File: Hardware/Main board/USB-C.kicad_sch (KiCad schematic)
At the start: 2 parts, among them P1 USB_C_Plug_USB2.0

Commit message: Big changes
- Folder changes
- change dimensions of board to match thicker material
- begin part selection/footprint selection
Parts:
- P1: footprint (none) -> Connector_USB:USB_C_Receptacle_HRO_TYPE-C-31-M-12; symbol Connector:USB_C_Plug_USB2.0 -> Connector:USB_C_Receptacle_USB2.0_14P
- R3: footprint (none) -> Resistor_SMD:R_0603_1608Metric
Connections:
- net D+: now also P1.B6 (D+)
- net D-: now also P1.B7 (D-)
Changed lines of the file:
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@@
 	(paper "A5")
+	(junction
+		(at 121.92 68.58)
+		(diameter 0)
+		(color 0 0 0 0)
+	)
 	(junction
 		(at 121.92 45.72)
@@
 		(color 0 0 0 0)
 	)
+	(junction
+		(at 121.92 63.5)
+		(diameter 0)
+		(color 0 0 0 0)
+	)
 	(no_connect
 		(at 121.92 58.42)
@@
 		(pts
 			(xy 124.46 68.58) (xy 121.92 68.58)
+		)
+		(stroke
+			(width 0)
+			(type default)
+		)
+	)
+	(wire
+		(pts
+			(xy 121.92 63.5) (xy 121.92 66.04)
+		)
+		(stroke
+			(width 0)
+			(type default)
+		)
+	)
+	(wire
+		(pts
+			(xy 121.92 68.58) (xy 121.92 71.12)
 		)
 		(stroke
@@
 	)
 	(symbol
-		(lib_id "Connector:USB_C_Plug_USB2.0")
+		(lib_id "Connector:USB_C_Receptacle_USB2.0_14P")
 		(at 106.68 66.04 0)
 		(unit 1)
@@
 			)
 		)
-		(property "Footprint" ""
+		(property "Footprint" "Connector_USB:USB_C_Receptacle_HRO_TYPE-C-31-M-12"
 			(at 110.49 66.04 0)
 			(effects
@@
 			)
 		)
-		(property "Description" "USB 2.0-only Type-C Plug connector"
+		(property "Description" "USB 2.0-only 14P Type-C Receptacle connector"
 			(at 106.68 66.04 0)
 			(effects
@@
 		)
 		(pin "S1"
+		)
+		(pin "B6"
+		)
+		(pin "B7"
 		)
 		(instances
@@
 			)
 		)
-		(property "Footprint" ""
+		(property "Footprint" "Resistor_SMD:R_0603_1608Metric"
 			(at 127 55.88 0)
 			(effects

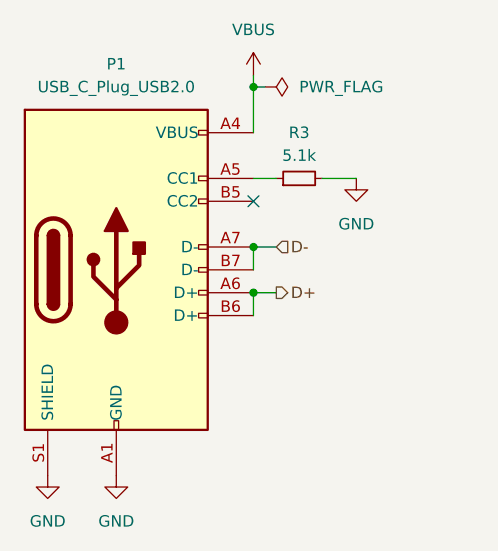
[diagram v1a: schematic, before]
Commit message: Schematic changes
- changed positions/schematic values and nets
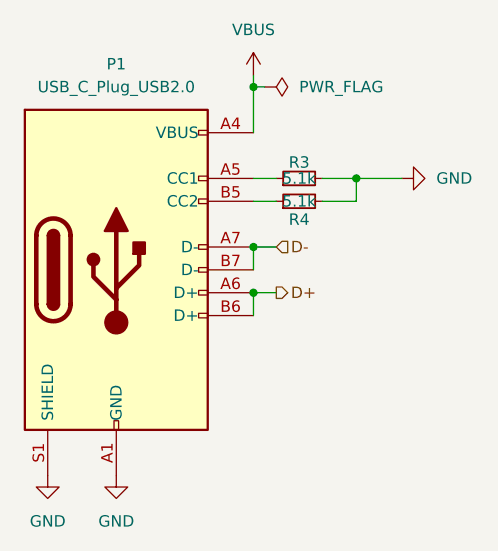
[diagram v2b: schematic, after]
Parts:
- added R4: 5.1k, Resistor_SMD:R_0603_1608Metric, symbol Device:R_Small
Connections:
- net GND: now also R4.2
- net at P1.B5 (CC2): now also R4.1
- no-connect marks 1 -> 0
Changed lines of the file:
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@@
 	(paper "A5")
+	(junction
+		(at 133.35 55.88)
+		(diameter 0)
+		(color 0 0 0 0)
+	)
 	(junction
 		(at 121.92 68.58)
@@
 		(color 0 0 0 0)
 	)
-	(no_connect
-		(at 121.92 58.42)
+	(wire
+		(pts
+			(xy 121.92 58.42) (xy 124.46 58.42)
+		)
+		(stroke
+			(width 0)
+			(type default)
+		)
 	)
 	(wire
@@
 	(wire
 		(pts
+			(xy 133.35 58.42) (xy 129.54 58.42)
+		)
+		(stroke
+			(width 0)
+			(type default)
+		)
+	)
+	(wire
+		(pts
+			(xy 133.35 55.88) (xy 129.54 55.88)
+		)
+		(stroke
+			(width 0)
+			(type default)
+		)
+	)
+	(wire
+		(pts
 			(xy 121.92 45.72) (xy 121.92 50.8)
 		)
@@
 	(wire
 		(pts
-			(xy 133.35 55.88) (xy 129.54 55.88)
+			(xy 133.35 55.88) (xy 133.35 58.42)
+		)
+		(stroke
+			(width 0)
+			(type default)
+		)
+	)
+	(wire
+		(pts
+			(xy 138.43 55.88) (xy 133.35 55.88)
 		)
 		(stroke
@@
 	(symbol
 		(lib_id "power:GND")
-		(at 133.35 55.88 0)
+		(at 138.43 55.88 90)
 		(unit 1)
 		(exclude_from_sim no)
@@
 		(dnp no)
 		(fields_autoplaced yes)
-		(property "Reference" "#PWR019"
-			(at 133.35 62.23 0)
+		(property "Reference" "#PWR017"
+			(at 144.78 55.88 0)
 			(effects
 				(font
@@
 		)
 		(property "Value" "GND"
-			(at 133.35 60.96 0)
-			(effects
-				(font
-					(size 1.27 1.27)
-				)
+			(at 142.24 55.8799 90)
+			(effects
+				(font
+					(size 1.27 1.27)
+				)
+				(justify right)
 			)
 		)
 		(property "Footprint" ""
-			(at 133.35 55.88 0)
+			(at 138.43 55.88 0)
 			(effects
 				(font
@@
 		)
 		(property "Datasheet" ""
-			(at 133.35 55.88 0)
+			(at 138.43 55.88 0)
 			(effects
 				(font
@@
 		)
 		(property "Description" "Power symbol creates a global label with name \"GND\" , ground"
-			(at 133.35 55.88 0)
+			(at 138.43 55.88 0)
 			(effects
 				(font
@@
 			(project "Minibadge Display 5x3"
 				(path "/e5119d15-74fb-4259-abbc-5cab1f368532/f82e88ca-9adc-48b9-bd3d-d05196ebe384"
-					(reference "#PWR019")
+					(reference "#PWR017")
 					(unit 1)
 				)
@@
 	)
 	(symbol
+		(lib_id "Device:R_Small")
+		(at 127 58.42 90)
+		(unit 1)
+		(exclude_from_sim no)
+		(in_bom yes)
+		(on_board yes)
+		(dnp no)
+		(property "Reference" "R4"
+			(at 127 60.452 90)
+			(effects
+				(font
+					(size 1.27 1.27)
+				)
+			)
+		)
+		(property "Value" "5.1k"
+			(at 127 58.42 90)
+			(effects
+				(font
+					(size 1.27 1.27)
+				)
+			)
+		)
+		(property "Footprint" "Resistor_SMD:R_0603_1608Metric"
+			(at 127 58.42 0)
+			(effects
+				(font
+					(size 1.27 1.27)
+				)
+				(hide yes)
+			)
+		)
+		(property "Datasheet" "~"
+			(at 127 58.42 0)
+			(effects
+				(font
+					(size 1.27 1.27)
+				)
+				(hide yes)
+			)
+		)
+		(property "Description" "Resistor, small symbol"
+			(at 127 58.42 0)
+			(effects
+				(font
+					(size 1.27 1.27)
+				)
+				(hide yes)
+			)
+		)
+		(pin "2"
+		)
+		(pin "1"
+		)
+		(instances
+			(project "Display main board"
+				(path "/e5119d15-74fb-4259-abbc-5cab1f368532/f82e88ca-9adc-48b9-bd3d-d05196ebe384"
+					(reference "R4")
+					(unit 1)
+				)
+			)
+		)
+	)
+	(symbol
 		(lib_id "Connector:USB_C_Receptacle_USB2.0_14P")
 		(at 106.68 66.04 0)
@@
 		(dnp no)
 		(fields_autoplaced yes)
-		(property "Reference" "#PWR018"
+		(property "Reference" "#PWR016"
 			(at 121.92 48.26 0)
 			(effects
@@
 			(project "Minibadge Display 5x3"
 				(path "/e5119d15-74fb-4259-abbc-5cab1f368532/f82e88ca-9adc-48b9-bd3d-d05196ebe384"
-					(reference "#PWR018")
+					(reference "#PWR016")
 					(unit 1)
 				)
@@
 		(dnp no)
 		(property "Reference" "R3"
-			(at 127 50.8 90)
+			(at 127 54.102 90)
 			(effects
 				(font
@@
 		)
 		(property "Value" "5.1k"
-			(at 127 53.34 90)
+			(at 127 55.88 90)
 			(effects
 				(font
@@
 		(dnp no)
 		(fields_autoplaced yes)
-		(property "Reference" "#PWR017"
+		(property "Reference" "#PWR015"
 			(at 106.68 95.25 0)
 			(effects
@@
 			(project "Minibadge Display 5x3"
 				(path "/e5119d15-74fb-4259-abbc-5cab1f368532/f82e88ca-9adc-48b9-bd3d-d05196ebe384"
-					(reference "#PWR017")
+					(reference "#PWR015")
 					(unit 1)
 				)
@@
 		(dnp no)
 		(fields_autoplaced yes)
-		(property "Reference" "#PWR016"
+		(property "Reference" "#PWR014"
 			(at 99.06 95.25 0)
 			(effects
@@
 			(project "Minibadge Display 5x3"
 				(path "/e5119d15-74fb-4259-abbc-5cab1f368532/f82e88ca-9adc-48b9-bd3d-d05196ebe384"
-					(reference "#PWR016")
-					(unit 1)
-				)
+					(reference "#PWR014")
+					(unit 1)
+				)

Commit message: hardware changes and initial traces/layout
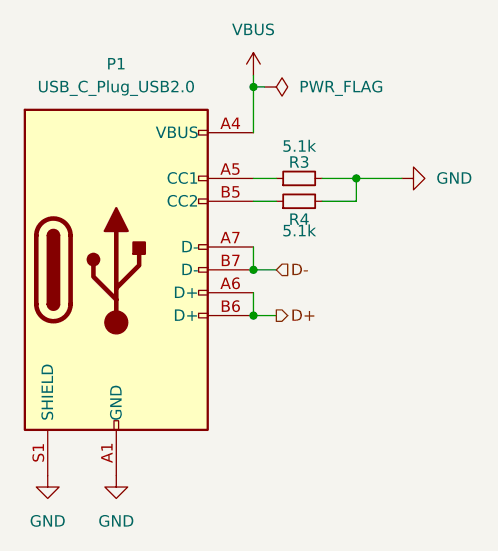
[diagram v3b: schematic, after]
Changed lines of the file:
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@@
 	)
 	(junction
-		(at 121.92 68.58)
+		(at 121.92 66.04)
 		(diameter 0)
 		(color 0 0 0 0)
@@
 	)
 	(junction
-		(at 121.92 63.5)
+		(at 121.92 71.12)
 		(diameter 0)
 		(color 0 0 0 0)
@@
 	(wire
 		(pts
+			(xy 121.92 71.12) (xy 124.46 71.12)
+		)
+		(stroke
+			(width 0)
+			(type default)
+		)
+	)
+	(wire
+		(pts
 			(xy 124.46 55.88) (xy 121.92 55.88)
 		)
@@
 	(wire
 		(pts
-			(xy 124.46 63.5) (xy 121.92 63.5)
-		)
-		(stroke
-			(width 0)
-			(type default)
-		)
-	)
-	(wire
-		(pts
-			(xy 124.46 68.58) (xy 121.92 68.58)
+			(xy 124.46 66.04) (xy 121.92 66.04)
 		)
 		(stroke
@@
 	(hierarchical_label "D-"
 		(shape input)
-		(at 124.46 63.5 0)
+		(at 124.46 66.04 0)
 		(effects
 			(font
@@
 	(hierarchical_label "D+"
 		(shape output)
-		(at 124.46 68.58 0)
+		(at 124.46 71.12 0)
 		(effects
 			(font
@@
 		)
 		(property "Value" "5.1k"
-			(at 127 58.42 90)
+			(at 127 61.722 90)
 			(effects
 				(font
@@
 		)
 		(property "Value" "5.1k"
-			(at 127 55.88 90)
-			(effects
-				(font
+			(at 127 52.324 90)
+			(effects
+				(font

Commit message: Part selection
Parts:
- P1: JLCPCB Part # (none) -> C165948; LCSC Part # (none) -> C165948
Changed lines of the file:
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@@
+			)
+		)
+		(property "JLCPCB Part #" "C165948"
+			(at 106.68 66.04 0)
+			(effects
+				(font
+					(size 1.27 1.27)
+				)
+				(hide yes)
+			)
+		)
+		(property "LCSC Part #" "C165948"
+			(at 106.68 66.04 0)
+			(effects
+				(font
+					(size 1.27 1.27)
+				)
+				(hide yes)
 			)
 		)

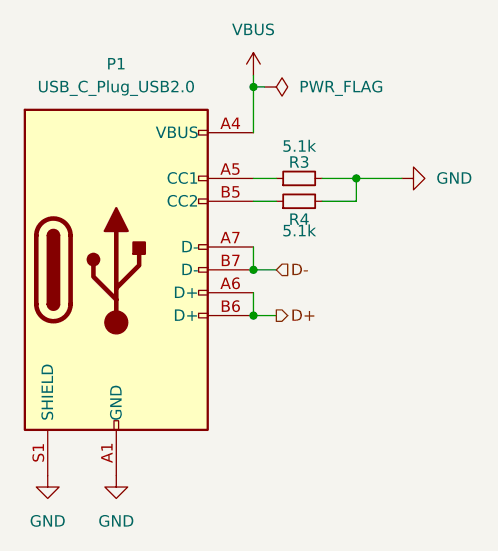
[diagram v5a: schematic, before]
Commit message: refactor PCB for new BMS layout
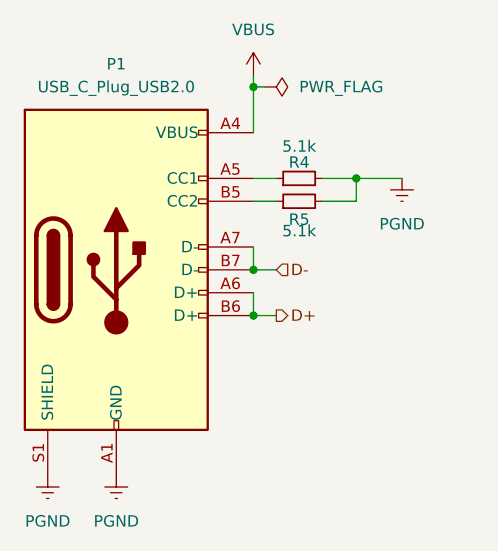
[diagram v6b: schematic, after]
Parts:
- renumbered R3 to R4, R4 to R5
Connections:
- net GND renamed PGND

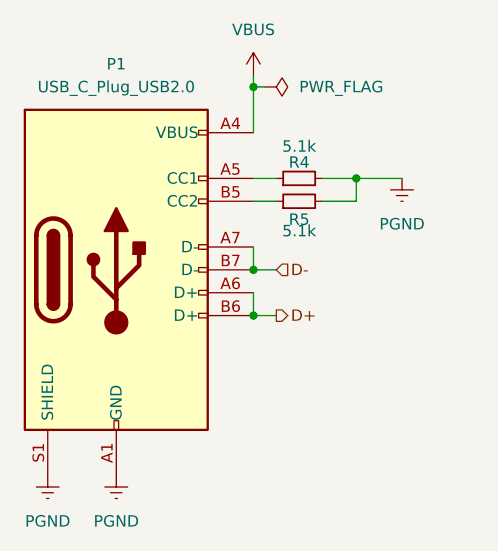
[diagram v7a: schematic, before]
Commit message: fix ohm s ymbol
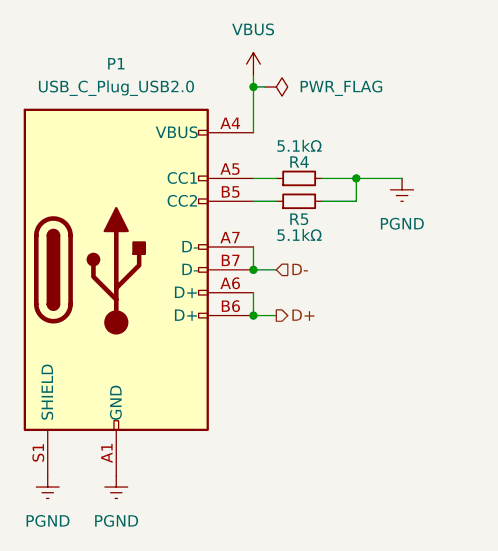
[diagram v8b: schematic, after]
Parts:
- R4, R5: value 5.1k -> 5.1kΩ
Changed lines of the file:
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@@
 			)
 		)
-		(property "Value" "5.1k"
-			(at 127 61.722 90)
+		(property "Value" "5.1kΩ"
+			(at 127 62.23 90)
 			(effects
 				(font
@@
 		)
 		(property "Design guide" ""
+			(at 127 58.42 0)
+			(effects
+				(font
+					(size 1.27 1.27)
+				)
+				(hide yes)
+			)
+		)
+		(property "JLCPCB Parts URL" ""
+			(at 127 58.42 0)
+			(effects
+				(font
+					(size 1.27 1.27)
+				)
+				(hide yes)
+			)
+		)
+		(property "LCSC Part #" ""
 			(at 127 58.42 0)
 			(effects
@@
 			)
 		)
-		(property "Value" "5.1k"
+		(property "Value" "5.1kΩ"
 			(at 127 52.324 90)
 			(effects
@@
 			(at 127 55.88 0)
 			(effects
+				(font
+					(size 1.27 1.27)
+				)
+				(hide yes)
+			)
+		)
+		(property "JLCPCB Parts URL" ""
+			(at 127 55.88 0)
+			(effects
+				(font
+					(size 1.27 1.27)
+				)
+				(hide yes)
+			)
+		)
+		(property "LCSC Part #" ""
+			(at 127 55.88 0)
+			(effects
